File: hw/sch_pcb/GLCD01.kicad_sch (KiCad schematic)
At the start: 8 parts, among them J1 Umin ... Umax, M1 HOLE M3, M2 HOLE M3, M3 HOLE, M4 HOLE

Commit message: v1 with mic1557
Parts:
- removed C1: 10uF, Capacitor_SMD:C_0805_2012Metric, symbol ISM02A-rescue:C_Small-Device-ISM02A-rescue
- removed C2: 100nF, Capacitor_SMD:C_0805_2012Metric, symbol ISM02A-rescue:C_Small-Device-ISM02A-rescue
- removed D1: BZV55C-5,6V, Diode_SMD:D_SMA, symbol ISM02A-rescue:D_ZENER-MLAB_D
- removed J1: Umin ... Umax, Mlab_Pin_Headers:Straight_2x03, symbol header:HEADER_2x03_PARALLEL
- added C2: GRM21BR71H105KA12L, Capacitor_SMD:C_0603_1608Metric, symbol Device:C_Small
- added C3, C4: 100nF/63V, Capacitor_SMD:C_0603_1608Metric, symbol Device:C_Small
- added J1: JUMP_7X2, Mlab_Pin_Headers:Straight_2x07, symbol MLAB_Jumpers:JUMP_7X2
- added J2: 046824610000846+, 046824610000846, symbol FPC_10:046824610000846+
- added Q1: BSS138, Package_TO_SOT_SMD:SOT-23, symbol Transistor_FET:BSS138
- added R1: 750k, Resistor_SMD:R_0603_1608Metric, symbol Device:R_Small
- added R2, R4: 1M, Resistor_SMD:R_0603_1608Metric, symbol Device:R_Small
- added R3: 1k, Resistor_SMD:R_0603_1608Metric, symbol Device:R_Small
- added U1: MIC1557YM5-TR, Package_TO_SOT_SMD:SOT-23-5, symbol MIC1557:MIC1557YM5-TR
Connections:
- net GND: now also C2.2, C3.2, C4.2, J1.13 (14), J1.14, J2.2, J2.7, Q1.2 (S), R4.2, U1.2 (GND)
- new net: Q1.3 (D), R2.2, U1.3 (CS)
- new net: J1.10, J1.9 (10), J2.6
- new net: J1.11 (12), J1.12, R3.1
- new net: J1.3 (4), J1.4, J2.3
- new net: J1.5 (6), J1.6, J2.4
- new net: J1.7 (8), J1.8, J2.5
- new net: Q1.1 (G), R3.2, R4.1
- new net: J2.9, R1.1, U1.5 (OUT)
- new net: C2.1, R1.2, U1.1 (T/T)
- new net +3.3V: C3.1, C4.1, J1.1 (2), J1.2, J2.1, J2.8, R2.1, U1.4 (VS)
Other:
- note removed: "Adjust power voltage range and symbol"
- note removed: "Delete if unused."
- note removed: "POWER INPUT"

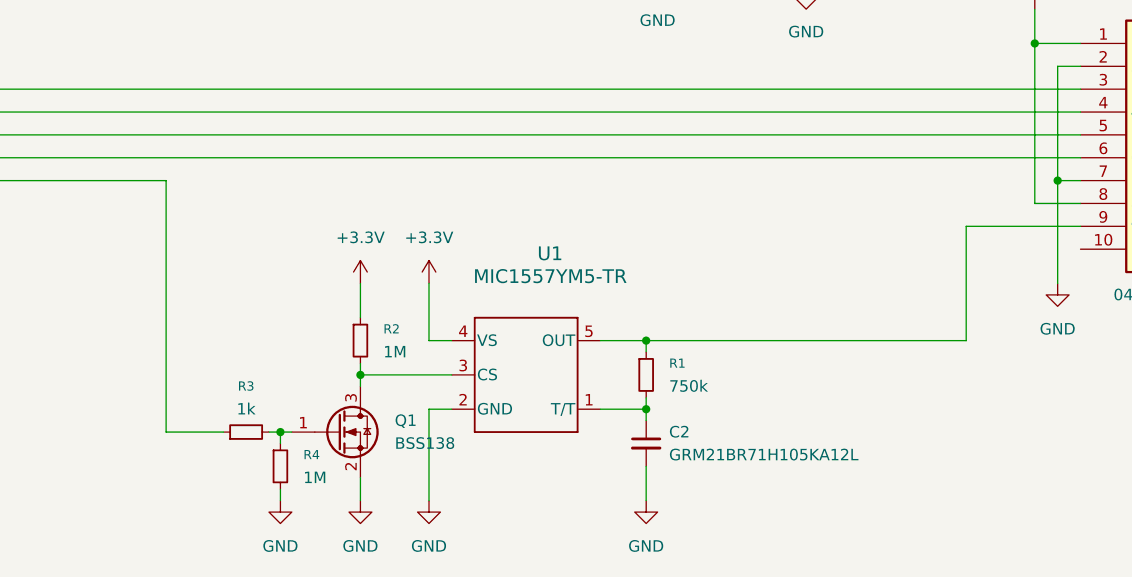
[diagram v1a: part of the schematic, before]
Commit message: Add MIC1557 circuit to schematic and update PCB layout
- Added R5 (0R, DNP) resistor to schematic
- Rearranged component placement on PCB
- Updated project file to newer KiCAD format
- Fixed author email in schematic title block
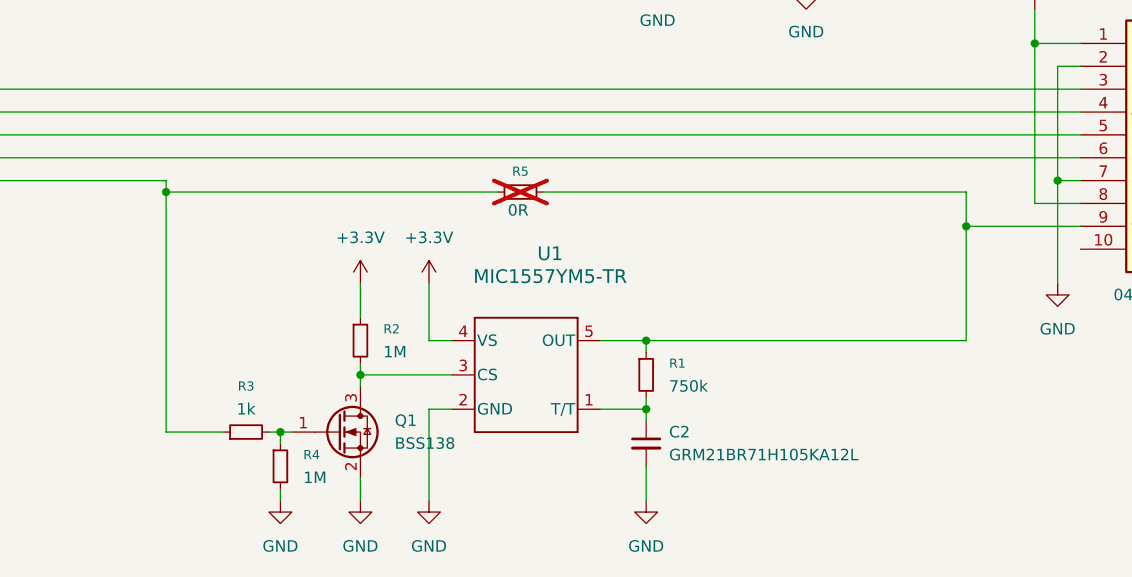
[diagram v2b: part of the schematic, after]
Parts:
- added R5: 0R, Resistor_SMD:R_0603_1608Metric, symbol Device:R_Small
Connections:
- net at J1.11 (12), J1.12, R3.1: now also R5.1
- net at J2.9, R1.1, U1.5 (OUT): now also R5.2
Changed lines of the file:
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@@
 		(company "Mlab www.mlab.cz")
 		(comment 1 "Square MIP LCD display module ")
-		(comment 2 "R-R <email@example.com>")
+		(comment 2 "R-R <r.roztocil@email.cz>")
 	)
 	(text "MOUNTING HOLES"
@@
 	)
 	(junction
+		(at 191.77 114.3)
+		(diameter 0)
+		(color 0 0 0 0)
+	)
+	(junction
 		(at 199.39 93.98)
 		(diameter 0)
@@
 		(color 0 0 0 0)
 	)
+	(junction
+		(at 102.87 110.49)
+		(diameter 0)
+		(color 0 0 0 0)
+	)
 	(wire
 		(pts
@@
 	(wire
 		(pts
+			(xy 191.77 110.49) (xy 191.77 114.3)
+		)
+		(stroke
+			(width 0)
+			(type default)
+		)
+	)
+	(wire
+		(pts
 			(xy 134.62 127) (xy 132.08 127)
 		)
@@
 	(wire
 		(pts
-			(xy 102.87 137.16) (xy 102.87 109.22)
+			(xy 102.87 137.16) (xy 102.87 110.49)
 		)
 		(stroke
@@
 	(wire
 		(pts
+			(xy 144.78 110.49) (xy 191.77 110.49)
+		)
+		(stroke
+			(width 0)
+			(type default)
+		)
+	)
+	(wire
+		(pts
 			(xy 157.48 83.82) (xy 157.48 86.36)
 		)
@@
 	(wire
 		(pts
+			(xy 102.87 110.49) (xy 139.7 110.49)
+		)
+		(stroke
+			(width 0)
+			(type default)
+		)
+	)
+	(wire
+		(pts
 			(xy 204.47 96.52) (xy 201.93 96.52)
 		)
@@
 			(width 0)
 			(type dash)
+		)
+	)
+	(wire
+		(pts
+			(xy 102.87 110.49) (xy 102.87 109.22)
+		)
+		(stroke
+			(width 0)
+			(type default)
 		)
 	)
@@
 					(unit 1)
 				)
+			)
+		)
+	)
+	(symbol
+		(lib_id "Device:R_Small")
+		(at 142.24 110.49 90)
+		(unit 1)
+		(exclude_from_sim no)
+		(in_bom yes)
+		(on_board yes)
+		(dnp yes)
+		(property "Reference" "R5"
+			(at 142.24 108.204 90)
+			(effects
+				(font
+					(size 1.016 1.016)
+				)
+			)
+		)
+		(property "Value" "0R"
+			(at 141.986 112.522 90)
+			(effects
+				(font
+					(size 1.27 1.27)
+				)
+			)
+		)
+		(property "Footprint" "Resistor_SMD:R_0603_1608Metric"
+			(at 142.24 110.49 0)
+			(effects
+				(font
+					(size 1.27 1.27)
+				)
+				(hide yes)
+			)
+		)
+		(property "Datasheet" "~"
+			(at 142.24 110.49 0)
+			(effects
+				(font
+					(size 1.27 1.27)
+				)
+				(hide yes)
+			)
+		)
+		(property "Description" "Resistor, small symbol"
+			(at 142.24 110.49 0)
+			(effects
+				(font
+					(size 1.27 1.27)
+				)
+				(hide yes)
+			)
+		)
+		(pin "1"
+		)
+		(pin "2"
+		)
+		(instances
+			(project "GLCD01"
+				(path "/2ae32537-a16f-4c5b-a56b-c6dddfb8ddb4"
+					(reference "R5")
+					(unit 1)
+				)

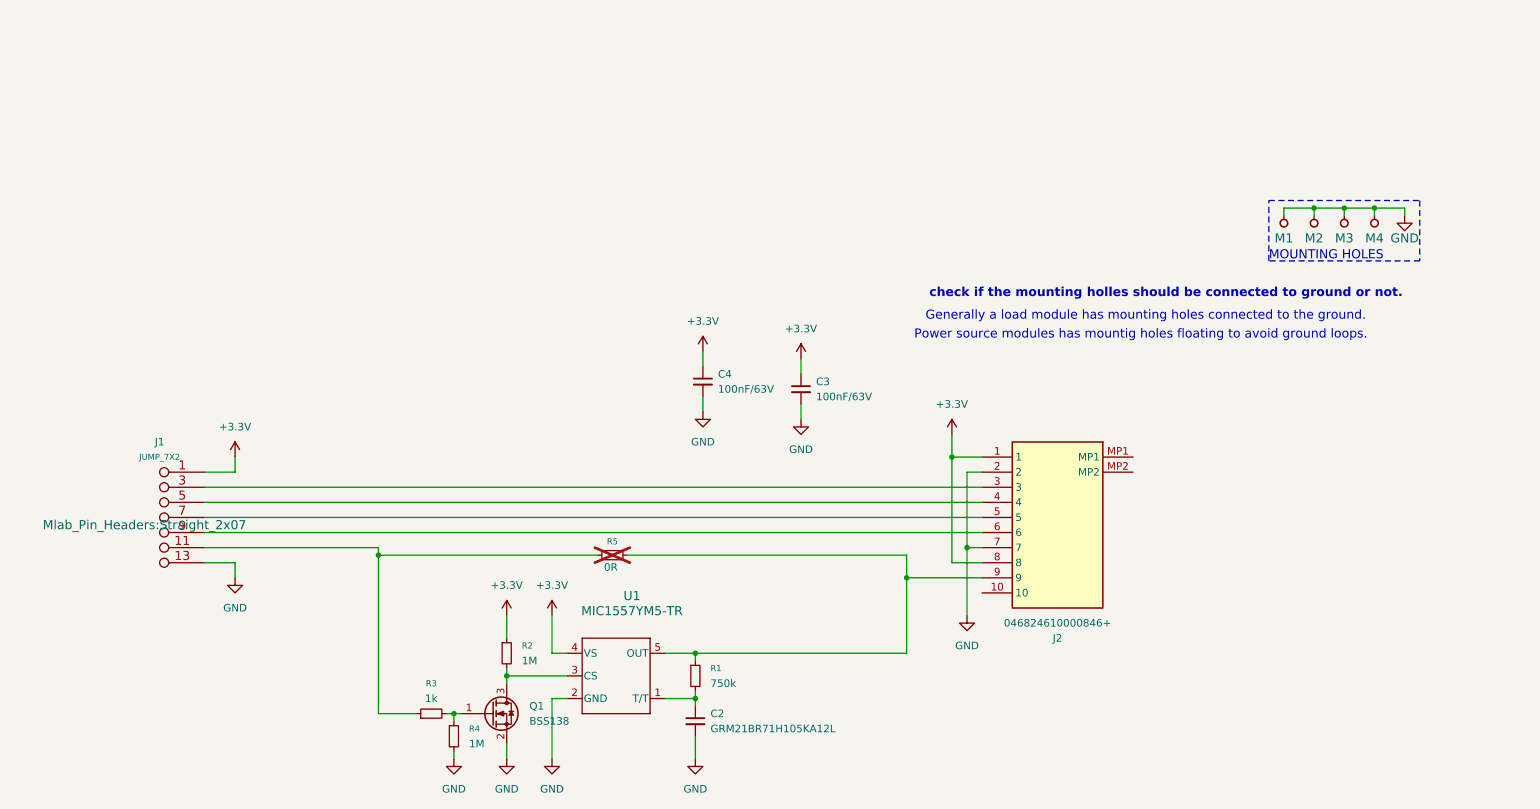
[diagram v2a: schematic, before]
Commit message: fix schematics, improve layout, thicker traces, update layout, add polarity protection, ...
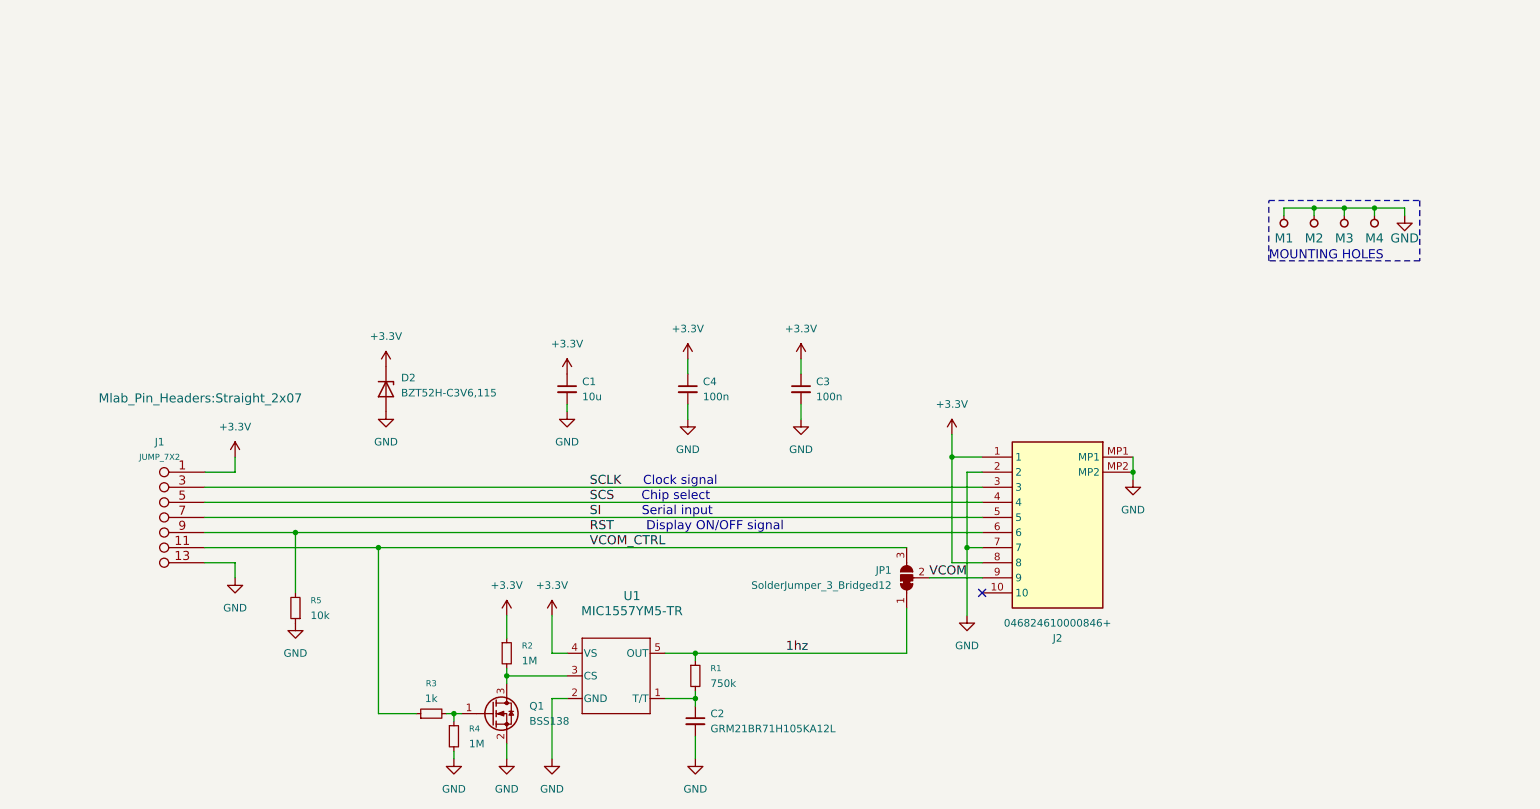
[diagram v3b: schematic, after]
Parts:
- added C1: 10u, Capacitor_SMD:C_0603_1608Metric, symbol Device:C_Small
- added D2: BZT52H-C3V6,115, Diode_SMD:D_SOD-123F, symbol Device:D_Zener
- added JP1: SolderJumper_3_Bridged12, Jumper:SolderJumper-3_P1.3mm_Bridged12_RoundedPad1.0x1.5mm, symbol Jumper:SolderJumper_3_Bridged12
- C3, C4: value 100nF/63V -> 100n
- R5: value 0R -> 10k; now fitted
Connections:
- net +3.3V: now also C1.1, D2.1 (K)
- net GND: now also J2.MP1, J2.MP2, R5.1, C1.2, D2.2 (A)
- net RST: now reaches J1.10, J1.9 (10), J2.6
- net RST: now also R5.2
- net VCOM_CTRL: now reaches J1.11 (12), J1.12, R3.1
- net VCOM_CTRL: now also JP1.3 (B); no longer R5.1
- net SCLK: now reaches J1.3 (4), J1.4, J2.3
- net SCS: now reaches J1.5 (6), J1.6, J2.4
- net SI: now reaches J1.7 (8), J1.8, J2.5
- net 1hz: now reaches R1.1, U1.5 (OUT)
- net 1hz: now also JP1.1 (A); no longer J2.9, R5.2
- new net VCOM: J2.9, JP1.2 (C)
- no-connect marks 0 -> 1
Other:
- note added: "Chip select"
- note added: "Clock signal"
- note added: "Display ON/OFF signal"
- note added: "Serial input"
- note removed: "Generally a load module has mounting holes connected to the ground."
- note removed: "Power source modules has mountig holes floating to avoid ground loops."
- note removed: "check if the mounting holles should be connected to ground or not."
- moved on the sheet: C4
